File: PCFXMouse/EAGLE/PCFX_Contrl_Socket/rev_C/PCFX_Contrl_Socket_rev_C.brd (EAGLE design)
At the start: 13.7 x 21.6 mm, 8 parts

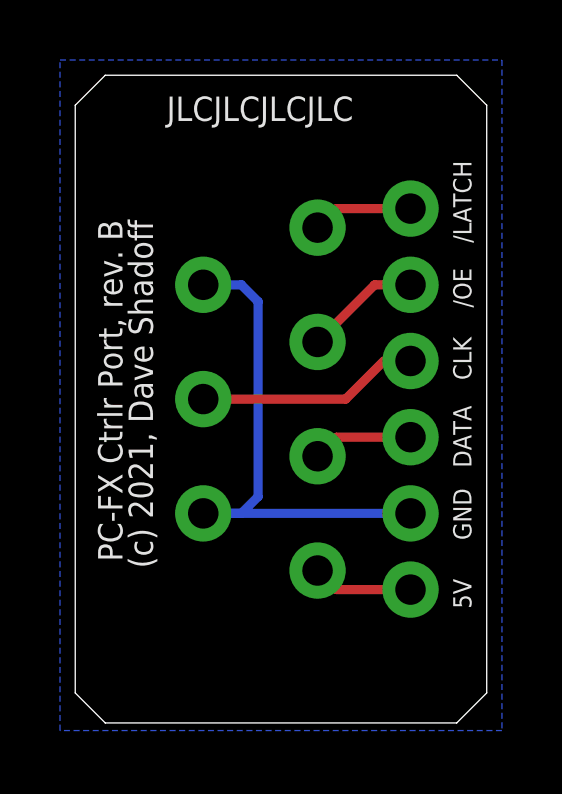
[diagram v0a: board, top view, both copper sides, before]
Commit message: Update FXMouse to KB2040 version
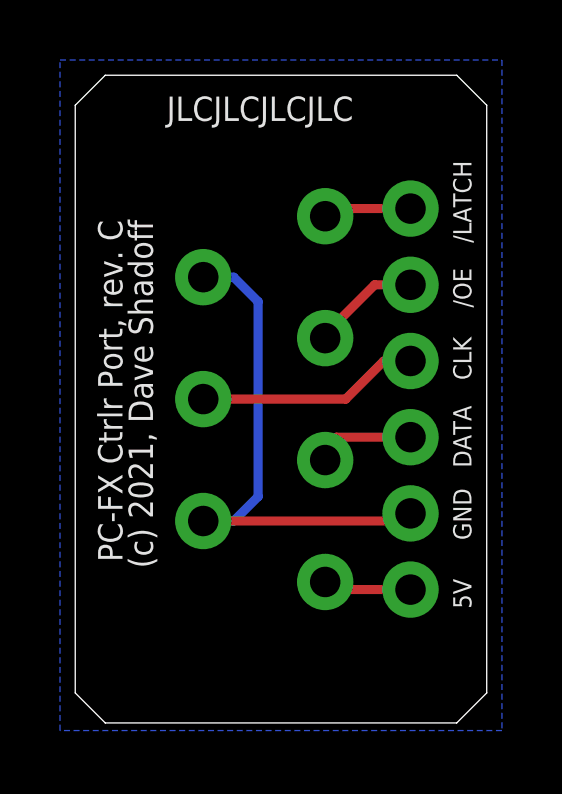
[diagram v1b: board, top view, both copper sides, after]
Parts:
- moved J1 0.46 mm to (8.33, 4.70)
- moved J4 0.46 mm to (8.33, 16.9)
- moved J2 0.28 mm to (8.33, 8.76)
- moved J3 0.28 mm to (8.33, 12.8)
- moved J5 0.25 mm to (4.27, 6.73)
- moved J7 0.25 mm to (4.27, 14.9)
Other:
- board text added: "PC-FX Ctrlr Port, rev. C"
- board text removed: "PC-FX Ctrlr Port, rev. B"
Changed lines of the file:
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@@
 <text x="13.208" y="13.843" size="0.6096" layer="25" rot="R90">/OE</text>
 <text x="13.208" y="16.002" size="0.6096" layer="25" rot="R90">/LATCH</text>
-<text x="0.762" y="16.764" size="0.8128" layer="25" rot="R270">PC-FX Ctrlr Port, rev. B</text>
+<text x="0.762" y="16.764" size="0.8128" layer="25" rot="R270">PC-FX Ctrlr Port, rev. C</text>
 <text x="1.778" y="16.764" size="0.8128" layer="25" rot="R270">(c) 2021, Dave Shadoff</text>
 <text x="3.048" y="20.066" size="0.8128" layer="25">JLCJLCJLCJLC</text>
@@
 </autorouter>
 <elements>
-<element name="J1" library="SparkFun-Connectors" library_urn="urn:adsk.eagle:library:513" package="1X01_NO_SILK" package3d_urn="urn:adsk.eagle:package:38041/1" value="" x="8.0772" y="5.08" smashed="yes">
-<attribute name="VALUE" x="6.8072" y="3.302" size="0.6096" layer="27" font="vector" ratio="20"/>
-</element>
-<element name="J2" library="SparkFun-Connectors" library_urn="urn:adsk.eagle:library:513" package="1X01_NO_SILK" package3d_urn="urn:adsk.eagle:package:38041/1" value="" x="8.0772" y="8.89" smashed="yes">
-<attribute name="VALUE" x="6.8072" y="7.112" size="0.6096" layer="27" font="vector" ratio="20"/>
-</element>
-<element name="J3" library="SparkFun-Connectors" library_urn="urn:adsk.eagle:library:513" package="1X01_NO_SILK" package3d_urn="urn:adsk.eagle:package:38041/1" value="" x="8.0772" y="12.7" smashed="yes">
-<attribute name="VALUE" x="6.8072" y="10.922" size="0.6096" layer="27" font="vector" ratio="20"/>
-</element>
-<element name="J4" library="SparkFun-Connectors" library_urn="urn:adsk.eagle:library:513" package="1X01_NO_SILK" package3d_urn="urn:adsk.eagle:package:38041/1" value="" x="8.0772" y="16.51" smashed="yes">
-<attribute name="VALUE" x="6.8072" y="14.732" size="0.6096" layer="27" font="vector" ratio="20"/>
-</element>
-<element name="J5" library="SparkFun-Connectors" library_urn="urn:adsk.eagle:library:513" package="1X01_NO_SILK" package3d_urn="urn:adsk.eagle:package:38041/1" value="" x="4.2672" y="6.985" smashed="yes">
-<attribute name="VALUE" x="2.9972" y="5.207" size="0.6096" layer="27" font="vector" ratio="20"/>
+<element name="J1" library="SparkFun-Connectors" library_urn="urn:adsk.eagle:library:513" package="1X01_NO_SILK" package3d_urn="urn:adsk.eagle:package:38041/1" value="" x="8.3312" y="4.699" smashed="yes">
+<attribute name="VALUE" x="7.0612" y="2.921" size="0.6096" layer="27" font="vector" ratio="20"/>
+</element>
+<element name="J2" library="SparkFun-Connectors" library_urn="urn:adsk.eagle:library:513" package="1X01_NO_SILK" package3d_urn="urn:adsk.eagle:package:38041/1" value="" x="8.3312" y="8.763" smashed="yes">
+<attribute name="VALUE" x="7.0612" y="6.985" size="0.6096" layer="27" font="vector" ratio="20"/>
+</element>
+<element name="J3" library="SparkFun-Connectors" library_urn="urn:adsk.eagle:library:513" package="1X01_NO_SILK" package3d_urn="urn:adsk.eagle:package:38041/1" value="" x="8.3312" y="12.827" smashed="yes">
+<attribute name="VALUE" x="7.0612" y="11.049" size="0.6096" layer="27" font="vector" ratio="20"/>
+</element>
+<element name="J4" library="SparkFun-Connectors" library_urn="urn:adsk.eagle:library:513" package="1X01_NO_SILK" package3d_urn="urn:adsk.eagle:package:38041/1" value="" x="8.3312" y="16.891" smashed="yes">
+<attribute name="VALUE" x="7.0612" y="15.113" size="0.6096" layer="27" font="vector" ratio="20"/>
+</element>
+<element name="J5" library="SparkFun-Connectors" library_urn="urn:adsk.eagle:library:513" package="1X01_NO_SILK" package3d_urn="urn:adsk.eagle:package:38041/1" value="" x="4.2672" y="6.731" smashed="yes">
+<attribute name="VALUE" x="2.9972" y="4.953" size="0.6096" layer="27" font="vector" ratio="20"/>
 </element>
 <element name="J6" library="SparkFun-Connectors" library_urn="urn:adsk.eagle:library:513" package="1X01_NO_SILK" package3d_urn="urn:adsk.eagle:package:38041/1" value="" x="4.2672" y="10.795" smashed="yes">
 <attribute name="VALUE" x="2.9972" y="9.017" size="0.6096" layer="27" font="vector" ratio="20"/>
 </element>
-<element name="J7" library="SparkFun-Connectors" library_urn="urn:adsk.eagle:library:513" package="1X01_NO_SILK" package3d_urn="urn:adsk.eagle:package:38041/1" value="" x="4.2672" y="14.605" smashed="yes">
-<attribute name="VALUE" x="2.9972" y="12.827" size="0.6096" layer="27" font="vector" ratio="20"/>
+<element name="J7" library="SparkFun-Connectors" library_urn="urn:adsk.eagle:library:513" package="1X01_NO_SILK" package3d_urn="urn:adsk.eagle:package:38041/1" value="" x="4.2672" y="14.859" smashed="yes">
+<attribute name="VALUE" x="2.9972" y="13.081" size="0.6096" layer="27" font="vector" ratio="20"/>
 </element>
 <element name="J9" library="SparkFun-Connectors" library_urn="urn:adsk.eagle:library:513" package="1X06_NO_SILK" package3d_urn="urn:adsk.eagle:package:38130/1" value="" x="11.176" y="17.145" smashed="yes" rot="R270">
@@
 <contactref element="J5" pad="1"/>
 <contactref element="J9" pad="5"/>
-<wire x1="4.2672" y1="14.605" x2="5.5372" y2="14.605" width="0.3048" layer="16"/>
-<wire x1="6.096" y1="14.0462" x2="5.5372" y2="14.605" width="0.3048" layer="16"/>
-<wire x1="6.096" y1="7.5438" x2="5.5372" y2="6.985" width="0.3048" layer="16"/>
-<wire x1="5.5372" y1="6.985" x2="4.2672" y2="6.985" width="0.3048" layer="16"/>
 <wire x1="6.096" y1="14.0462" x2="6.096" y2="7.5438" width="0.3048" layer="16"/>
-<wire x1="4.2672" y1="6.985" x2="11.176" y2="6.985" width="0.3048" layer="16"/>
+<wire x1="6.096" y1="14.0462" x2="5.2832" y2="14.859" width="0.3048" layer="16"/>
+<wire x1="5.2832" y1="14.859" x2="4.2672" y2="14.859" width="0.3048" layer="16"/>
+<wire x1="6.096" y1="7.5438" x2="5.2832" y2="6.731" width="0.3048" layer="16"/>
+<wire x1="5.2832" y1="6.731" x2="4.2672" y2="6.731" width="0.3048" layer="16"/>
+<wire x1="4.2672" y1="6.731" x2="10.922" y2="6.731" width="0.3048" layer="1"/>
+<wire x1="10.922" y1="6.731" x2="11.176" y2="6.985" width="0.3048" layer="1"/>
 </signal>
 <signal name="N$1">
 <contactref element="J9" pad="1"/>
 <contactref element="J4" pad="1"/>
-<wire x1="8.0772" y1="16.51" x2="8.7122" y2="17.145" width="0.3048" layer="1"/>
-<wire x1="8.7122" y1="17.145" x2="11.176" y2="17.145" width="0.3048" layer="1"/>
+<wire x1="8.3312" y1="16.891" x2="8.5852" y2="17.145" width="0.3048" layer="1"/>
+<wire x1="8.5852" y1="17.145" x2="11.176" y2="17.145" width="0.3048" layer="1"/>
 </signal>
 <signal name="N$2">
 <contactref element="J9" pad="2"/>
 <contactref element="J3" pad="1"/>
-<wire x1="8.0772" y1="12.7" x2="9.9822" y2="14.605" width="0.3048" layer="1"/>
-<wire x1="9.9822" y1="14.605" x2="11.176" y2="14.605" width="0.3048" layer="1"/>
+<wire x1="11.176" y1="14.605" x2="9.9822" y2="14.605" width="0.3048" layer="1"/>
+<wire x1="9.9822" y1="14.605" x2="8.3312" y2="12.954" width="0.3048" layer="1"/>
+<wire x1="8.3312" y1="12.954" x2="8.3312" y2="12.827" width="0.3048" layer="1"/>
 </signal>
 <signal name="N$3">
@@
 <contactref element="J9" pad="4"/>
 <contactref element="J2" pad="1"/>
-<wire x1="8.0772" y1="8.89" x2="8.7122" y2="9.525" width="0.3048" layer="1"/>
 <wire x1="8.7122" y1="9.525" x2="11.176" y2="9.525" width="0.3048" layer="1"/>
+<wire x1="8.3312" y1="8.763" x2="8.3312" y2="9.144" width="0.3048" layer="1"/>
+<wire x1="8.3312" y1="9.144" x2="8.7122" y2="9.525" width="0.3048" layer="1"/>
 </signal>
 <signal name="N$5">
 <contactref element="J1" pad="1"/>
 <contactref element="J9" pad="6"/>
-<wire x1="8.0772" y1="5.08" x2="8.7122" y2="4.445" width="0.3048" layer="1"/>
 <wire x1="8.7122" y1="4.445" x2="11.176" y2="4.445" width="0.3048" layer="1"/>
+<wire x1="8.3312" y1="4.699" x2="8.4582" y2="4.699" width="0.3048" layer="1"/>
+<wire x1="8.4582" y1="4.699" x2="8.7122" y2="4.445" width="0.3048" layer="1"/>
 </signal>
 </signals>
